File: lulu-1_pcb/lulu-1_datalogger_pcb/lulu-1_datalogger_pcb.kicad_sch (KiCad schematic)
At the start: 40 parts, among them J1 SD_Card_Receptacle, J2 TYPE-C-31-M-12, J3 Conn_01x02_Pin, J4 Conn_01x20_Socket, SW1 SW_Nidec_CAS-120A1, U1 STM32F401RETx, U2 BMP280, U3 MPU-6050, U4 W25Q16JVSS, U5 LP3982ILD-3.3, Y1 25 Mhz, Y2 32 Khz

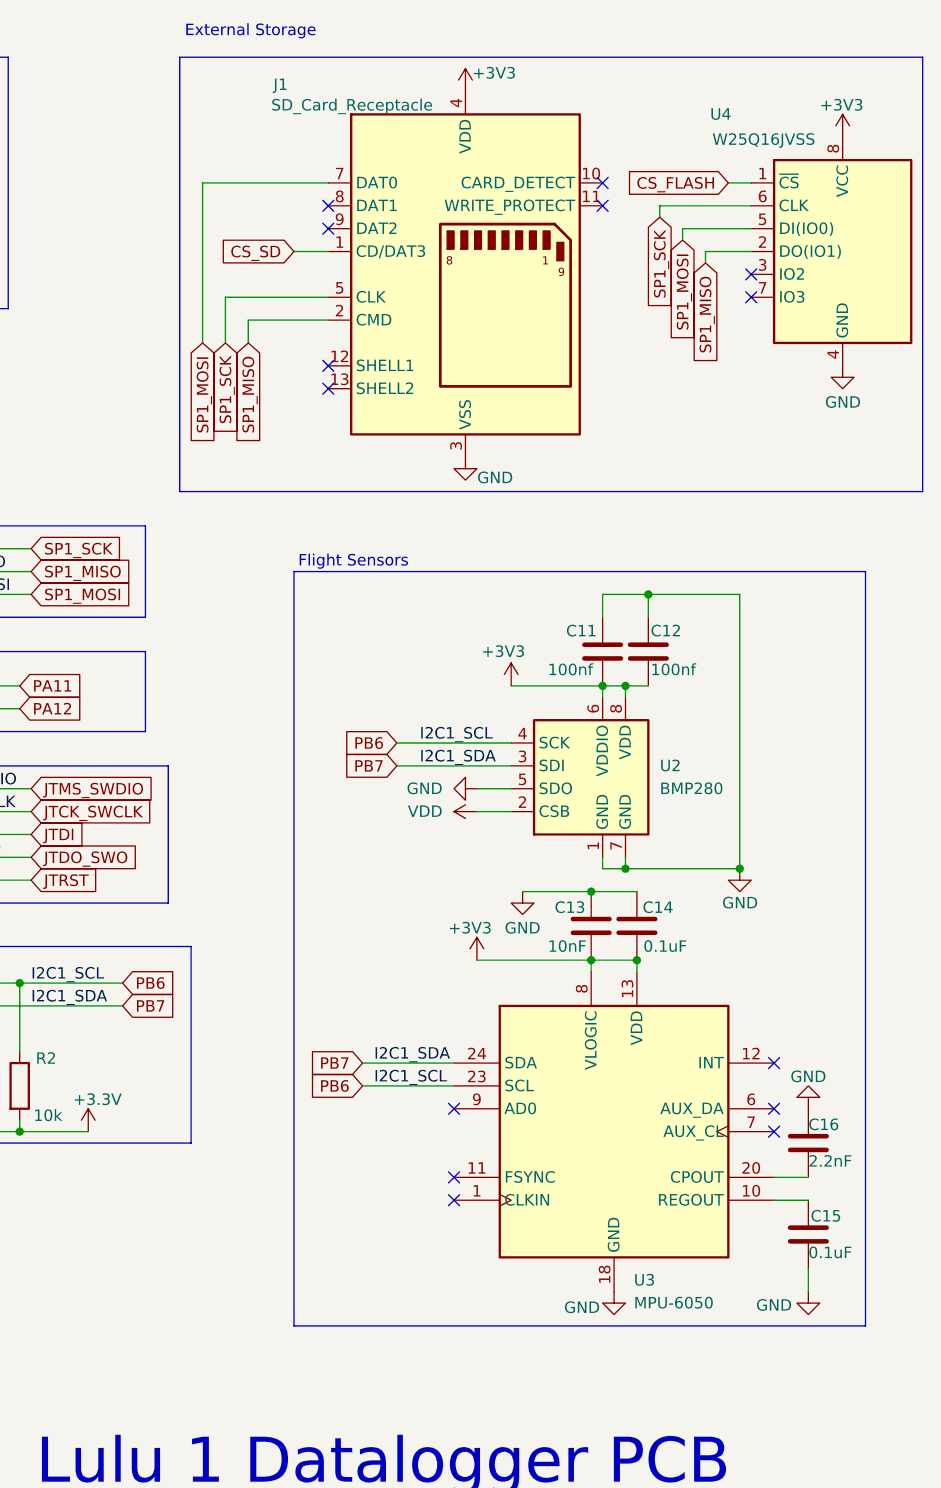
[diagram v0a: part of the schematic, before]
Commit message: imported and added hinged sd card with footprint
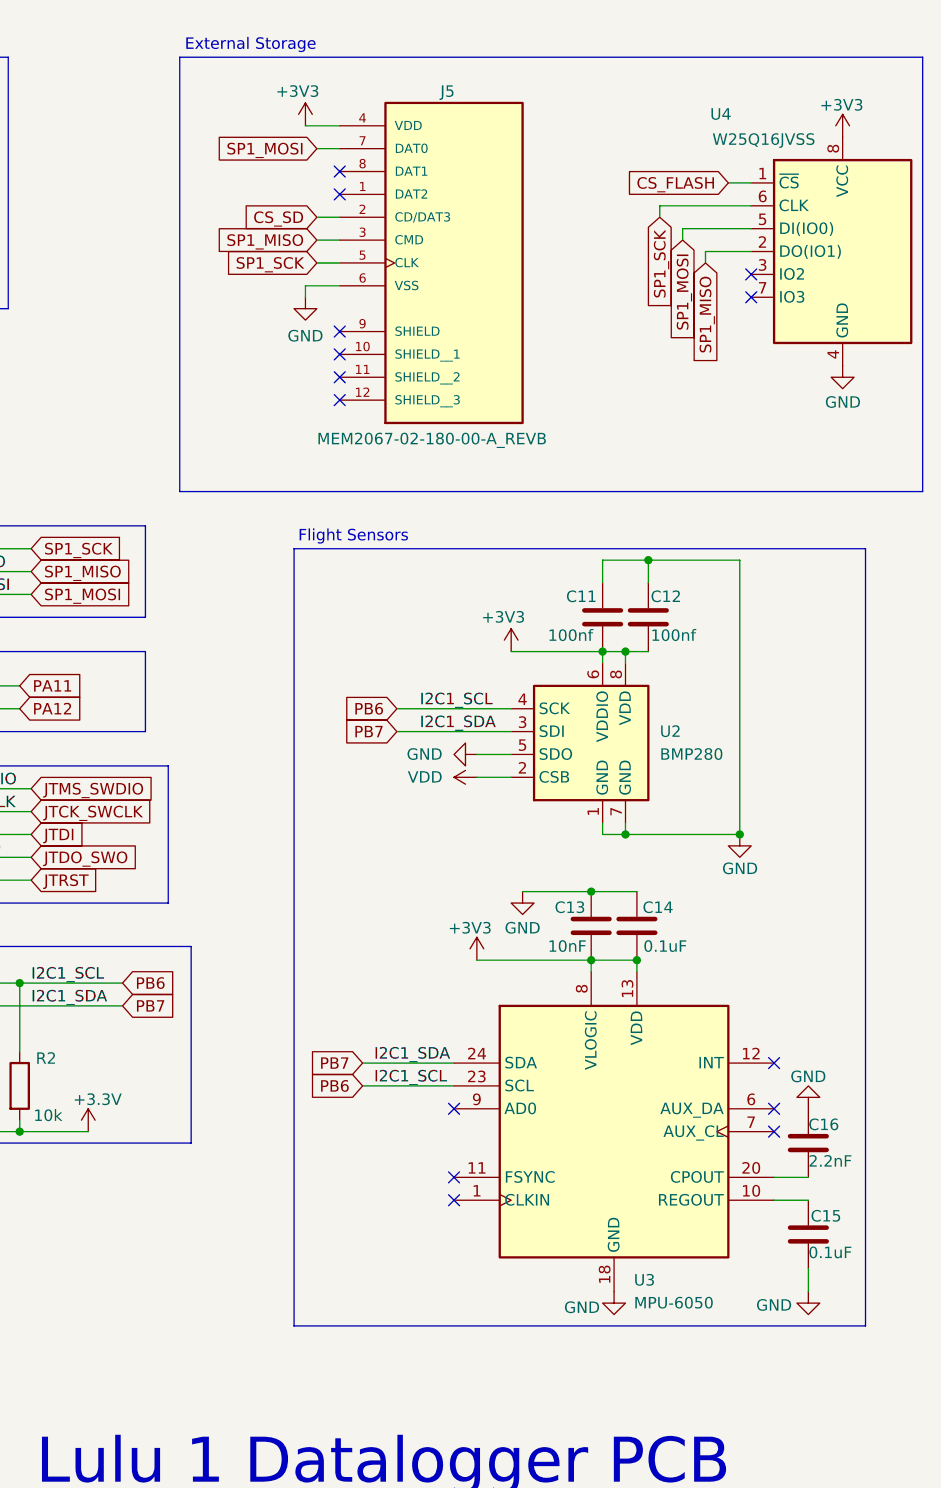
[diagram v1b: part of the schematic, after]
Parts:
- removed J1: SD_Card_Receptacle, Connector_Card:SD-SIM_microSD-microSIM_Molex_104168-1620, symbol Connector:SD_Card_Receptacle
- added J5: MEM2067-02-180-00-A_REVB, MEM2067-02-180-00-A_REVB:GCT_MEM2067-02-180-00-A_REVB, symbol MEM2067-02-180-00-A_REVB:MEM2067-02-180-00-A_REVB
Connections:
- net +3V3: now also J5.4 (VDD)
- net CS_SD: now also J5.2 (CD/DAT3)
- net GND: now also J5.6 (VSS)
- net SP1_MISO: now also J5.3 (CMD)
- net SP1_MOSI: now also J5.7 (DAT0)
- net SP1_SCK: now also J5.5 (CLK)
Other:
- moved on the sheet: C11, C12, U2

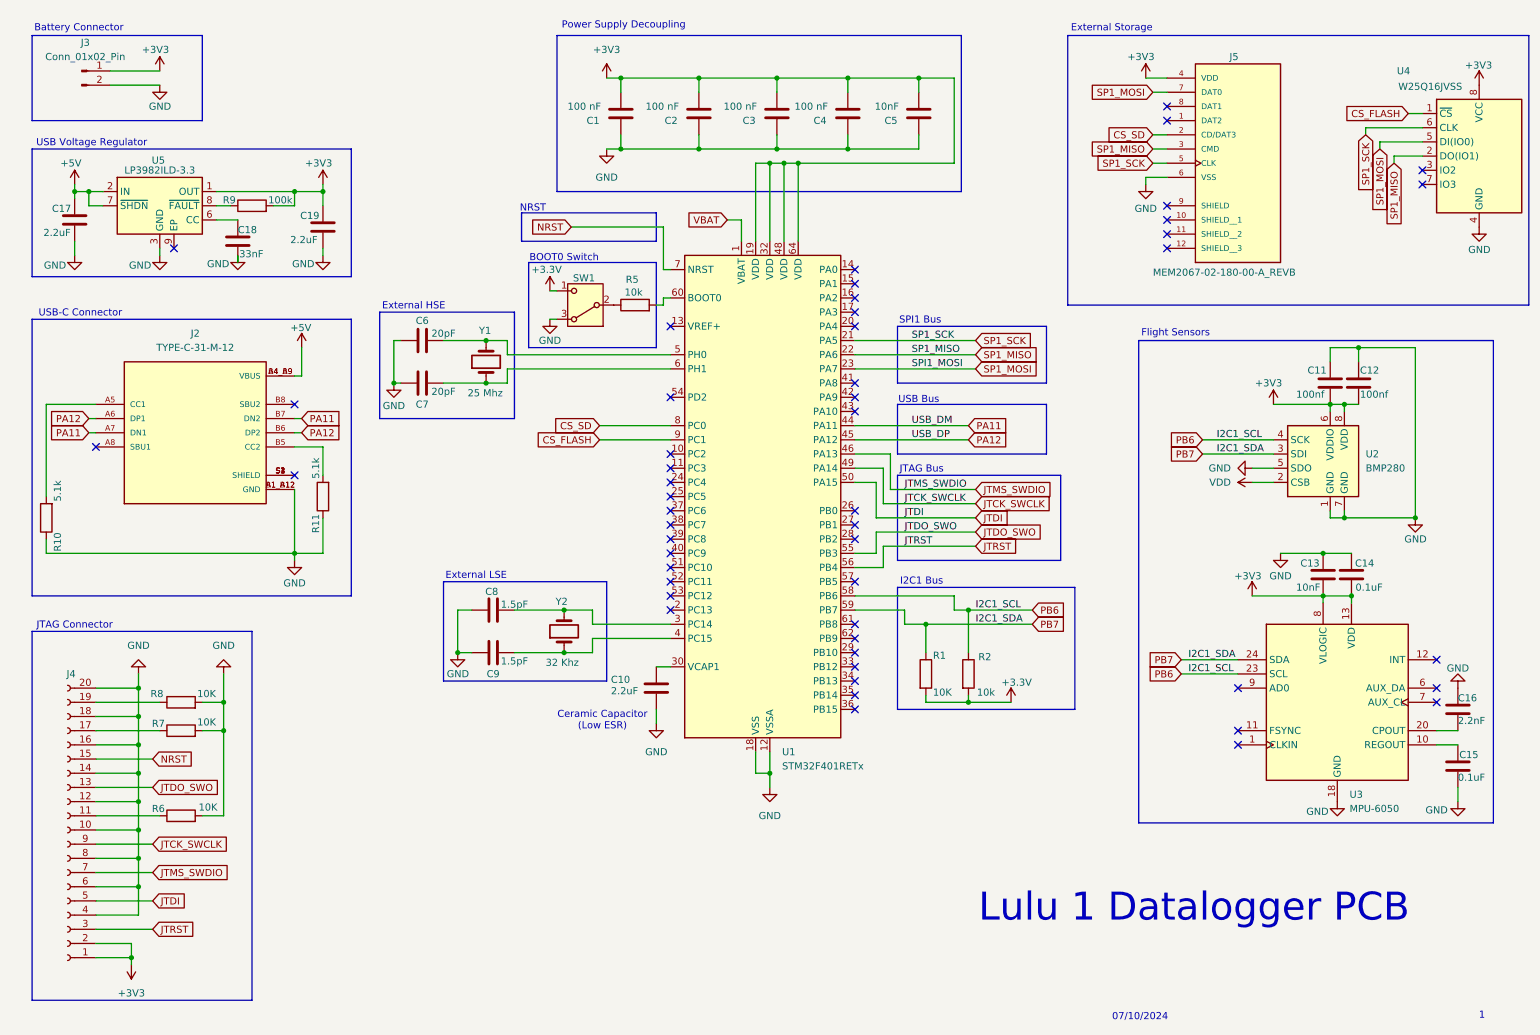
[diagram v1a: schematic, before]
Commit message: removed usb-c from schematic
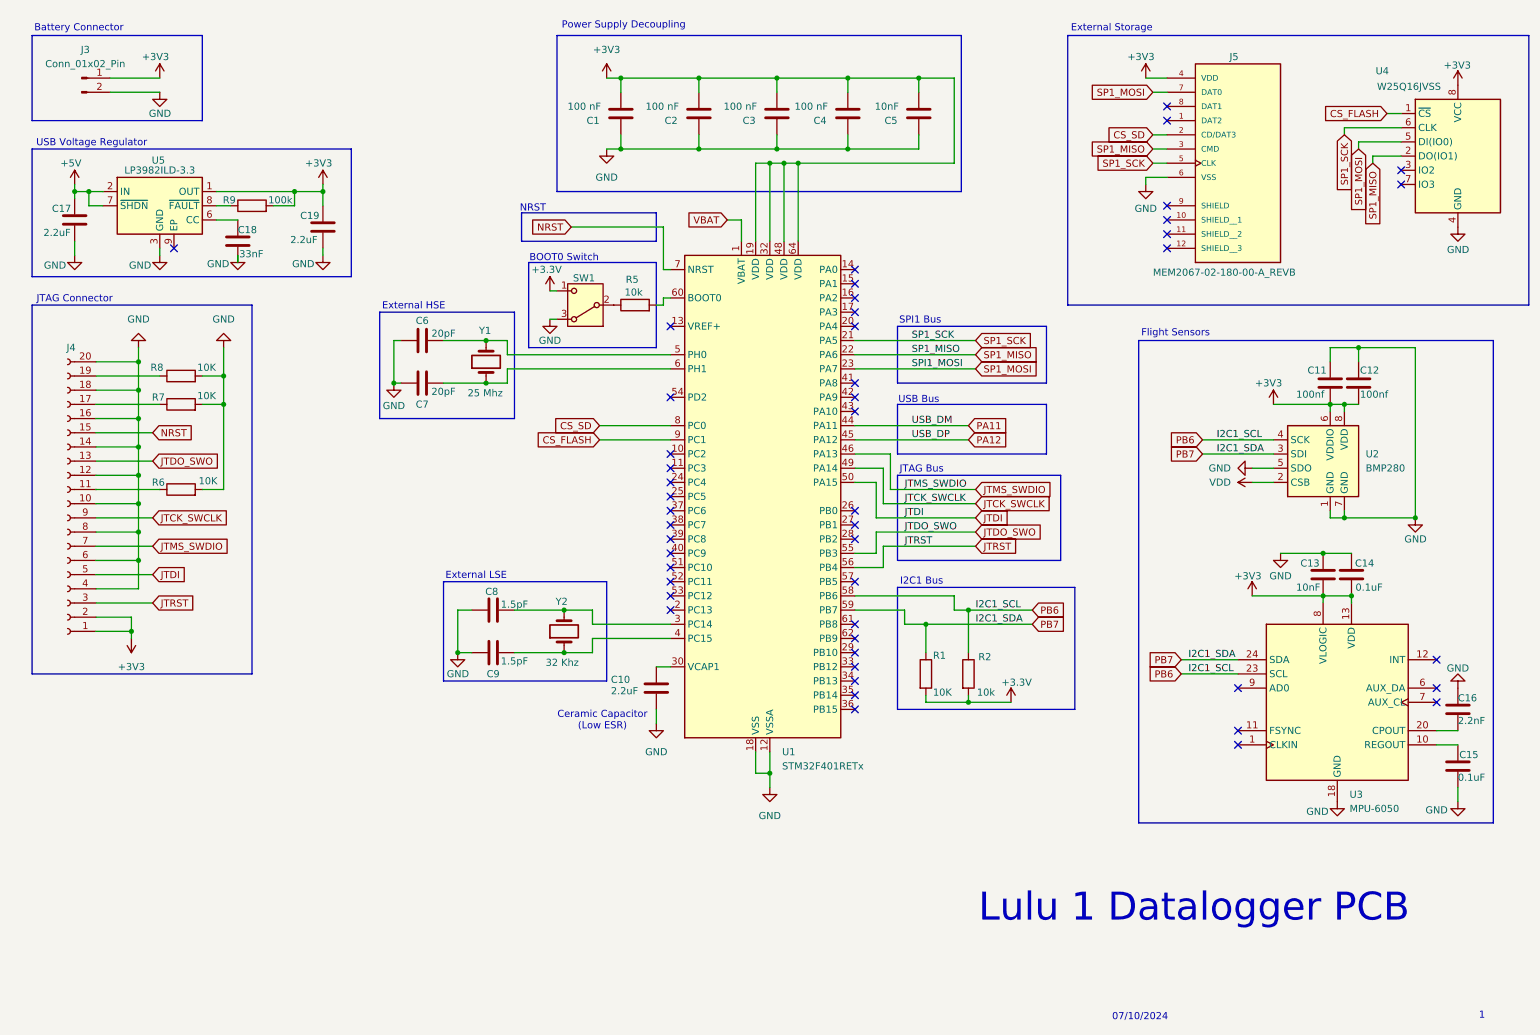
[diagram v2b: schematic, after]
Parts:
- removed J2: TYPE-C-31-M-12, TYPE-C-31-M-12:HRO_TYPE-C-31-M-12, symbol TYPE-C-31-M-12:TYPE-C-31-M-12
- removed R10, R11: 5.1k, Resistor_SMD:R_0805_2012Metric, symbol Device:R
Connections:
- no-connect marks 51 -> 48
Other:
- note removed: "USB-C Connector"
- moved on the sheet: J3, J4, R6, R7, R8, U4

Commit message: re-imported JTAG connector with symbol and footprint from manufacturer
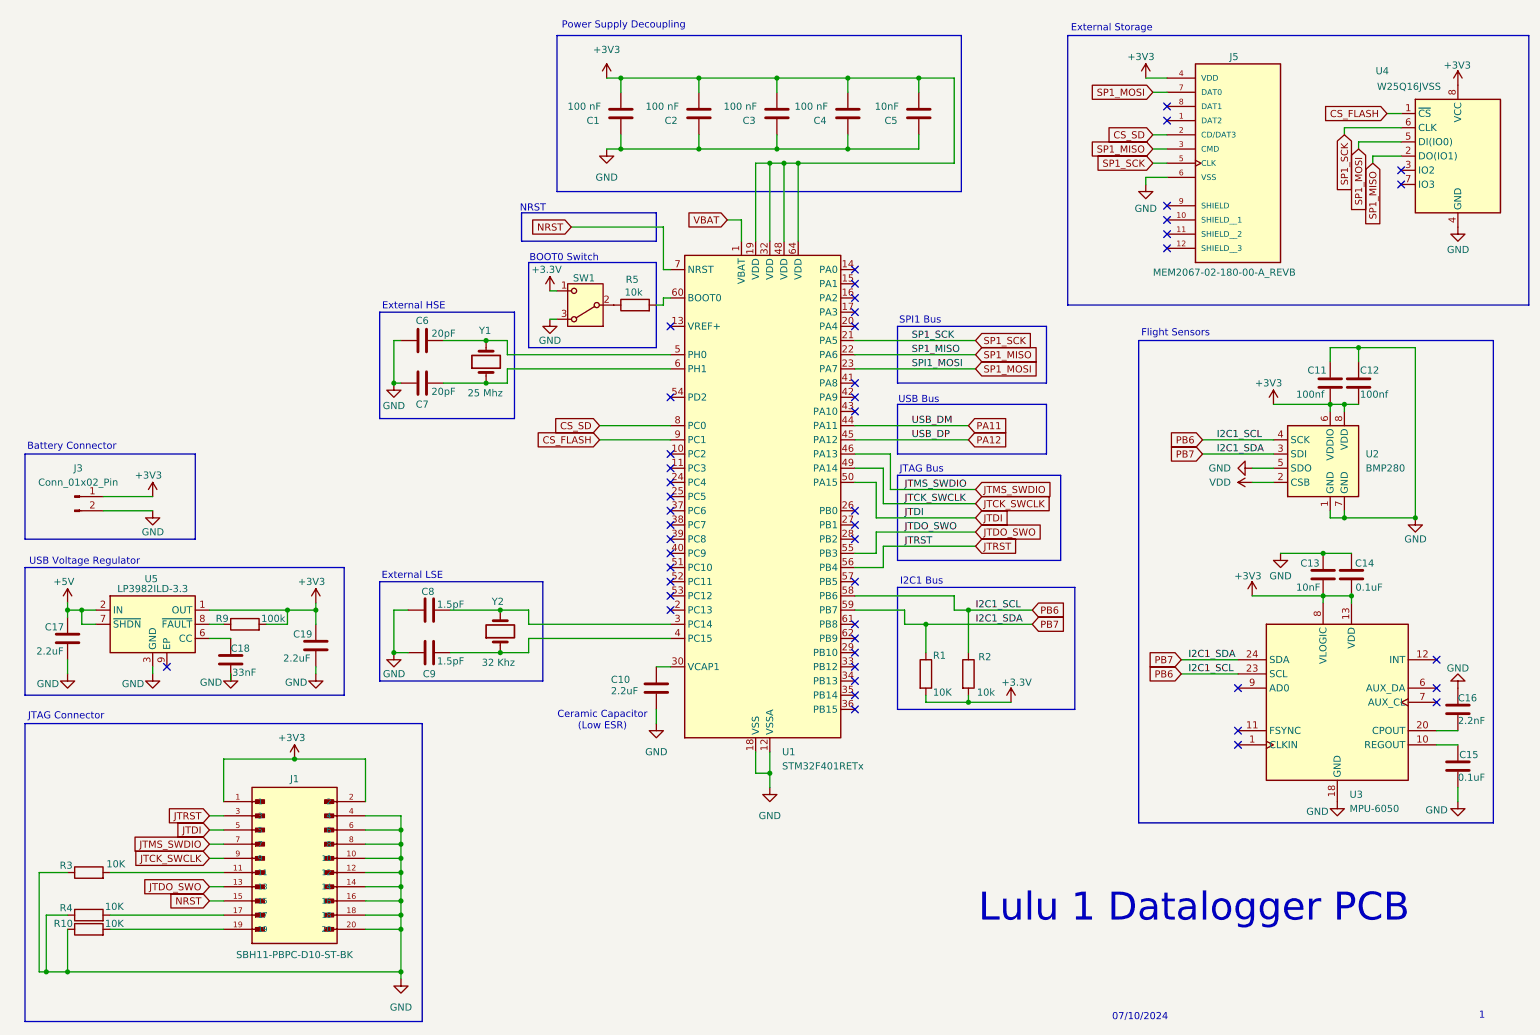
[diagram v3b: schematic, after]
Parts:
- removed J4: Conn_01x20_Socket, Connector:FanPinHeader_1x04_P2.54mm_Vertical, symbol Connector:Conn_01x20_Socket
- removed R6, R7, R8: 10K, Resistor_SMD:R_0805_2012Metric, symbol Device:R
- added J1: SBH11-PBPC-D10-ST-BK, SBH11-PBPC-D10-ST-BK:SULLINS_SBH11-PBPC-D10-ST-BK, symbol SBH11-PBPC-D10-ST-BK:SBH11-PBPC-D10-ST-BK
- added R10, R3, R4: 10K, Resistor_SMD:R_0805_2012Metric, symbol Device:R
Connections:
- net +3V3: now also J1.1, J1.2
- net GND: now also J1.10, J1.12, J1.14, J1.16, J1.18, J1.20, J1.4, J1.6, J1.8, R10.1, R3.1, R4.1
- net JTCK_SWCLK: now also J1.9
- net JTDI: now also J1.5
- net JTDO_SWO: now also J1.13
- net JTMS_SWDIO: now also J1.7
- net JTRST: now also J1.3
- net NRST: now also J1.15
- new net: J1.11, R3.2
- new net: J1.17, R4.2
- new net: J1.19, R10.2
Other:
- moved on the sheet: C17, C18, C19, C8, C9, J3, R9, U5, Y2

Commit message: reannotated schematic
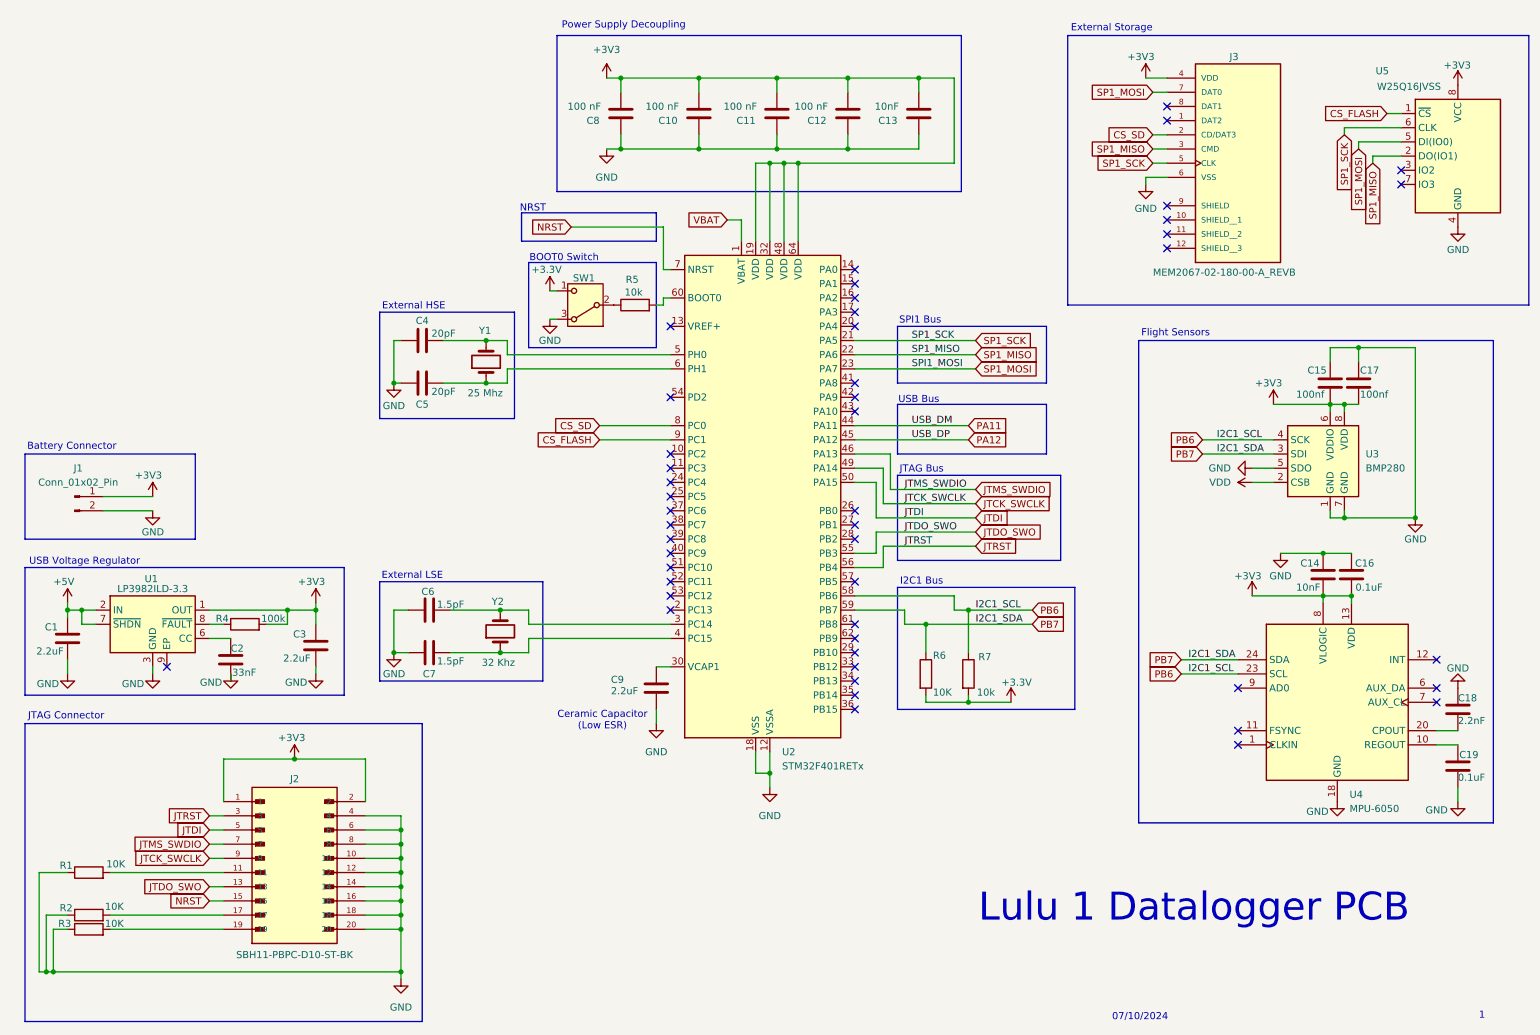
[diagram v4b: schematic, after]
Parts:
- renumbered C17 to C1, C2 to C10, C3 to C11, C4 to C12, C5 to C13, C13 to C14, C11 to C15, C14 to C16, C12 to C17, C16 to C18, C15 to C19, C18 to C2, C19 to C3, C6 to C4, C7 to C5, C8 to C6, C9 to C7, C1 to C8, C10 to C9, J3 to J1, J1 to J2, J5 to J3, R3 to R1, R4 to R2, R10 to R3, R9 to R4, R1 to R6, R2 to R7, U5 to U1, U1 to U2, U2 to U3, U3 to U4, U4 to U5
